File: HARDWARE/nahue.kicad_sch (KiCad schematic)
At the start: 42 parts, among them J1 Conn_01x15, J2 Screw_Terminal_01x03, J3 Screw_Terminal_01x03, J4 Screw_Terminal_01x03, J5 bateria, J6 Screw_Terminal_01x03, J7 Conn_01x15, K1 JQC-3FF-005-1Z, K2 JQC-3FF-005-1Z, K3 JQC-3FF-005-1Z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

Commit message: actualizacion de kicad
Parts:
- removed C2: C_Small, Capacitor_THT:C_Axial_L5.1mm_D3.1mm_P10.00mm_Horizontal, symbol Device:C_Small
- removed U5: KA78M05_TO252, Package_TO_SOT_SMD:TO-252-2, symbol Regulator_Linear:KA78M05_TO252
- added C2: C_Polarized, symbol Device:C_Polarized
- added U5: ESP32-S2-WROVER, RF_Module:ESP32-S2-WROVER, symbol RF_Module:ESP32-S2-WROVER
- added U6: LM7805_TO220, Package_TO_SOT_THT:TO-220-3_Vertical, symbol Regulator_Linear:LM7812_TO220
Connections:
- net +5V: now also C2.2; no longer C1.1
- net D19: now also R4.2; no longer R7.2
- net D21: now also R7.2; no longer R10.1
- net D22: now also R10.1
- net D5: no longer R4.2
- net GND: now also U6.2 (GND); no longer C1.2
- net at J5.2 (Pin_2): now also C1.1
- new net: C2.1, U6.3 (VO)
- new net: C1.2, U6.1 (VI)
- new net: U5.1 (GND), U5.26 (GND), U5.42 (GND), U5.43 (GND)
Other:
- moved on the sheet: C1, J5

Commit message: modificacion del kicad
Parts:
- removed U5: ESP32-S2-WROVER, RF_Module:ESP32-S2-WROVER, symbol RF_Module:ESP32-S2-WROVER
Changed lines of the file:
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@@
-	)
-	(symbol
-		(lib_id "RF_Module:ESP32-S2-WROVER")
-		(at -55.88 48.26 0)
-		(unit 1)
-		(exclude_from_sim no)
-		(in_bom yes)
-		(on_board yes)
-		(dnp no)
-		(fields_autoplaced yes)
-		(property "Reference" "U5"
-			(at -53.7367 15.24 0)
-			(effects
-				(font
-					(size 1.27 1.27)
-				)
-				(justify left)
-			)
-		)
-		(property "Value" "ESP32-S2-WROVER"
-			(at -53.7367 17.78 0)
-			(effects
-				(font
-					(size 1.27 1.27)
-				)
-				(justify left)
-			)
-		)
-		(property "Footprint" "RF_Module:ESP32-S2-WROVER"
-			(at -36.83 77.47 0)
-			(effects
-				(font
-					(size 1.27 1.27)
-				)
-				(hide yes)
-			)
-		)
-		(property "Datasheet" "https://www.espressif.com/sites/default/files/documentation/esp32-s2-wroom_esp32-s2-wroom-i_datasheet_en.pdf"
-			(at -63.5 68.58 0)
-			(effects
-				(font
-					(size 1.27 1.27)
-				)
-				(hide yes)
-			)
-		)
-		(property "Description" "RF Module, ESP32-D0WDQ6 SoC, Wi-Fi 802.11b/g/n, 32-bit, 2.7-3.6V, onboard antenna, SMD"
-			(at -55.88 48.26 0)
-			(effects
-				(font
-					(size 1.27 1.27)
-				)
-				(hide yes)
-			)
-		)
-		(pin "41"
-		)
-		(pin "32"
-		)
-		(pin "30"
-		)
-		(pin "18"
-		)
-		(pin "25"
-		)
-		(pin "22"
-		)
-		(pin "8"
-		)
-		(pin "11"
-		)
-		(pin "2"
-		)
-		(pin "13"
-		)
-		(pin "40"
-		)
-		(pin "36"
-		)
-		(pin "35"
-		)
-		(pin "4"
-		)
-		(pin "26"
-		)
-		(pin "37"
-		)
-		(pin "34"
-		)
-		(pin "27"
-		)
-		(pin "24"
-		)
-		(pin "3"
-		)
-		(pin "17"
-		)
-		(pin "6"
-		)
-		(pin "9"
-		)
-		(pin "16"
-		)
-		(pin "7"
-		)
-		(pin "15"
-		)
-		(pin "19"
-		)
-		(pin "5"
-		)
-		(pin "21"
-		)
-		(pin "10"
-		)
-		(pin "12"
-		)
-		(pin "14"
-		)
-		(pin "43"
-		)
-		(pin "39"
-		)
-		(pin "1"
-		)
-		(pin "42"
-		)
-		(pin "20"
-		)
-		(pin "38"
-		)
-		(pin "33"
-		)
-		(pin "31"
-		)
-		(pin "29"
-		)
-		(pin "28"
-		)
-		(pin "23"
-		)
-		(instances
-			(project ""
-				(path "/0a4955d6-c713-42be-8446-0591522708f4"
-					(reference "U5")
-					(unit 1)
-				)
-			)
-		)
 	)
 	(symbol

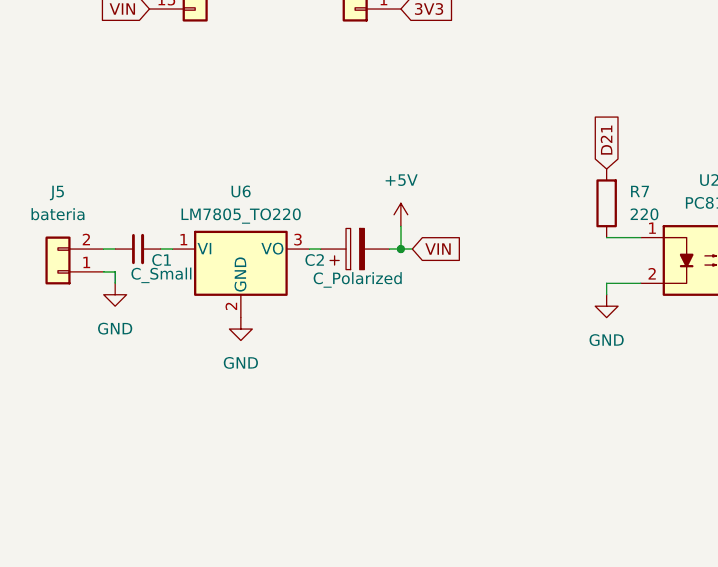
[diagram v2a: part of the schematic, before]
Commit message: modificacion de capacitores pararlelo
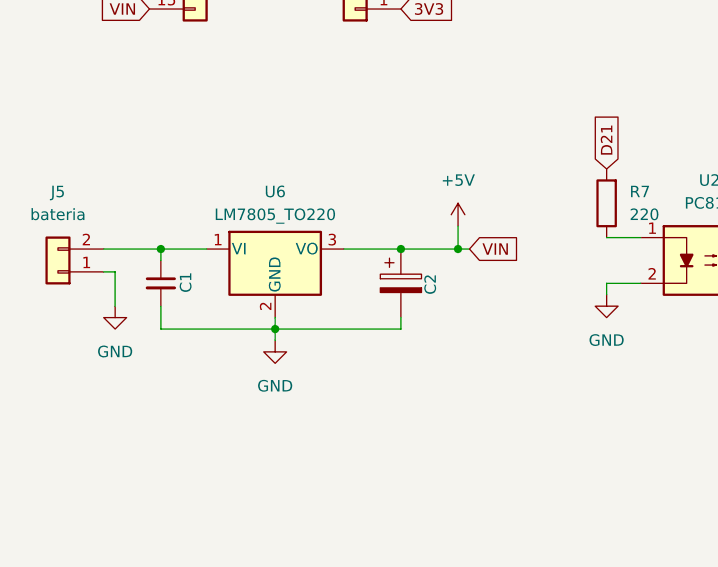
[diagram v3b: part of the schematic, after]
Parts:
- C1: value C_Small -> ~
- C2: value C_Polarized -> ~
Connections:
- net +5V: now also C2.1, U6.3 (VO); no longer C2.2
- net GND: now also C1.2, C2.2
- net at C1.1, J5.2 (Pin_2): now also U6.1 (VI)
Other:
- moved on the sheet: C1, C2, U6

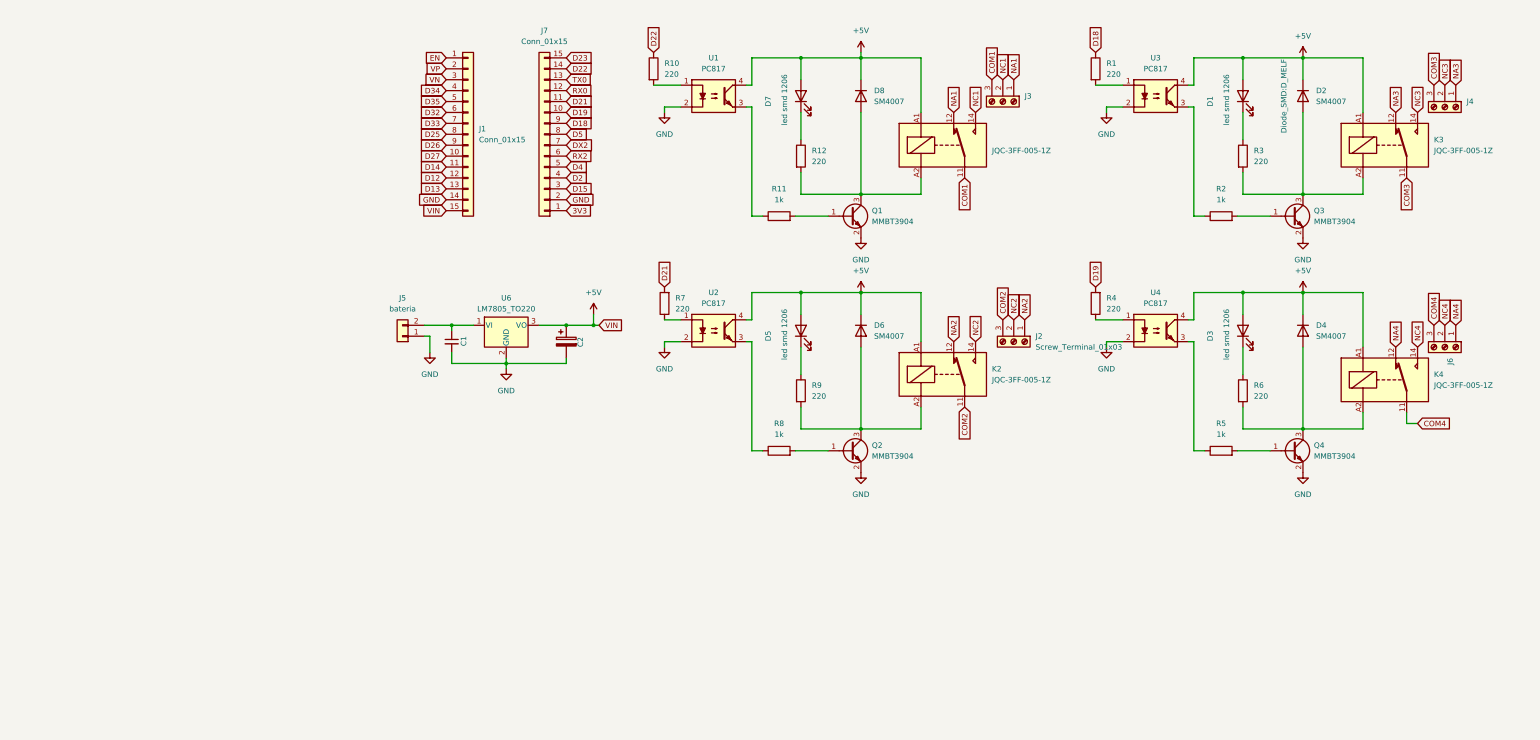
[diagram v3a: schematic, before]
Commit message: se agrego huella del ESP32(falta terminar)
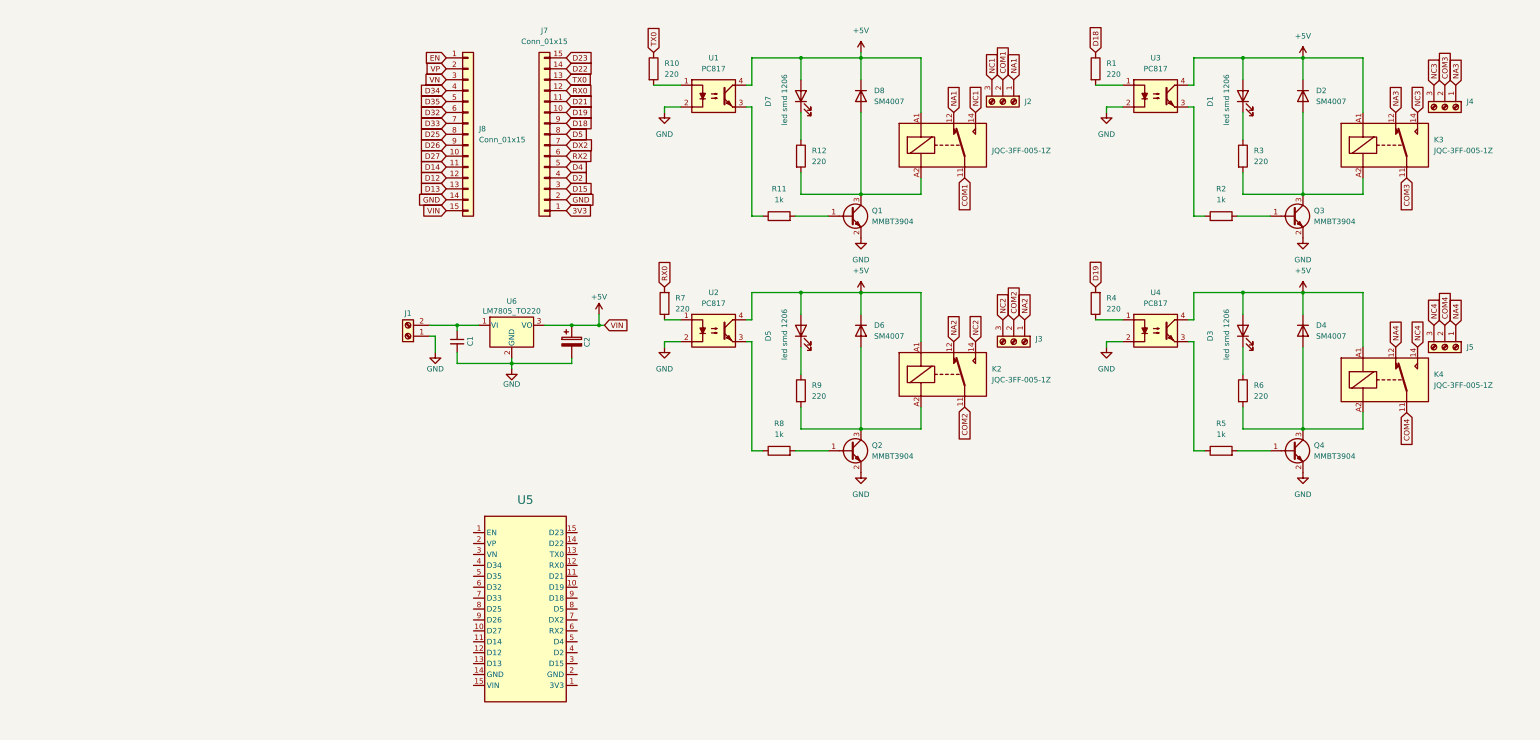
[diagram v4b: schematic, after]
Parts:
- removed J5: bateria, TerminalBlock:TerminalBlock_MaiXu_MX126-5.0-02P_1x02_P5.00mm, symbol Connector_Generic:Conn_01x02
- added J1: ~, TerminalBlock:TerminalBlock_MaiXu_MX126-5.0-02P_1x02_P5.00mm, symbol Connector:Screw_Terminal_01x02
- added U5: ~, esp32-30pines:esp32, symbol ESP32-devkiv v1:ESP32-30pines
- C2: footprint (none) -> Capacitor_THT:CP_Radial_D8.0mm_P3.80mm
- J3: renamed from J2; value Screw_Terminal_01x03 -> ~
- renumbered J3 to J2, J6 to J5, J1 to J8
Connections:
- net COM1: now also J2.2 (Pin_2); no longer J2.3 (Pin_3)
- net COM2: now also J3.2 (Pin_2); no longer J3.3 (Pin_3)
- net COM3: now also J4.2 (Pin_2); no longer J4.3 (Pin_3)
- net COM4: now also J5.2 (Pin_2); no longer J5.3 (Pin_3)
- net D21: no longer R7.2
- net D22: no longer R10.1
- net GND: now also J1.1 (Pin_1)
- net NC1: now also J2.3 (Pin_3); no longer J2.2 (Pin_2)
- net NC2: now also J3.3 (Pin_3); no longer J3.2 (Pin_2)
- net NC3: now also J4.3 (Pin_3); no longer J4.2 (Pin_2)
- net NC4: now also J5.3 (Pin_3); no longer J5.2 (Pin_2)
- net RX0: now also R7.2
- net TX0: now also R10.1
- net at C1.1, U6.1 (VI): now also J1.2 (Pin_2)
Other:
- moved on the sheet: C1, C2, U6

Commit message: últimos arreglos 1
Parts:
- removed J7, J8: Conn_01x15, Connector_PinHeader_2.54mm:PinHeader_1x15_P2.54mm_Vertical, symbol Connector_Generic:Conn_01x15
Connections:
- net +5V: now also U5.15 (VIN)
- net 3V3: now also U5.30 (3V3)
- net D12: now also U5.12 (D12)
- net D13: now also U5.13 (D13)
- net D14: now also U5.11 (D14)
- net D15: now also U5.28 (D15)
- net D18: now also U5.22 (D18)
- net D19: now also U5.21 (D19)
- net D2: now also U5.27 (D2)
- net D21: now also U5.20 (D21)
- net D22: now also U5.17 (D22)
- net D23: now also U5.16 (D23)
- net D25: now also U5.8 (D25)
- net D26: now also U5.9 (D26)
- net D27: now also U5.10 (D27)
- net D32: now also U5.6 (D32)
- net D33: now also U5.7 (D33)
- net D34: now also U5.4 (D34)
- net D35: now also U5.5 (D35)
- net D4: now also U5.26 (D4)
- net D5: now also U5.23 (D5)
- net DX2: now also R7.2, U5.24 (DX2)
- net EN: now also U5.1 (EN)
- net GND: now also U5.14 (GND), U5.29 (GND)
- net RX0: now also U5.19 (RX0); no longer R7.2
- net RX2: now also R10.1, U5.25 (RX2)
- net TX0: now also U5.18 (TX0); no longer R10.1
- net VN: now also U5.3 (VN)
- net VP: now also U5.2 (VP)
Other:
- moved on the sheet: U5

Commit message: retoques del kicad
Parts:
- K1, K2, K3, K4: value JQC-3FF-005-1Z -> RELAY
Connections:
- net DX2: no longer R7.2
- net RX0: now also R10.1
- net RX2: no longer R10.1
- net TX0: now also R7.2
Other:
- note added: "_"
- moved on the sheet: C1, C2, D1, D2, D3, D4, D5, D6, D7, D8, J1, J2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

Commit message: finalizando
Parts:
- added J6: Conn_01x08, Connector_PinSocket_2.54mm:PinSocket_1x08_P2.54mm_Vertical, symbol Connector_Generic:Conn_01x08
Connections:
- net +5V: now also J6.1 (Pin_1)
- net D18: now also R4.2; no longer R1.1
- net D19: now also R1.1; no longer R4.2
- net D2: now also J6.5 (Pin_5)
- net D22: now also J6.2 (Pin_2)
- net D25: now also J6.6 (Pin_6)
- net D32: now also J6.7 (Pin_7)
- net DX2: now also R7.2
- net RX0: now also J6.4 (Pin_4); no longer R10.1
- net RX2: now also R10.1
- net TX0: now also J6.3 (Pin_3); no longer R7.2
- net VP: now also J6.8 (Pin_8)

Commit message: finalizado 2
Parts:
- added SW1: SW, Connector_PinHeader_2.54mm:PinHeader_1x02_P2.54mm_Vertical, symbol Switch:SW_DPST_x2
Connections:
- net D18: no longer R4.2
- net D19: now also R4.2; no longer R1.1
- net D23: now also R1.1
- net at C1.1, U6.1 (VI): now also SW1.2 (B); no longer J1.2 (Pin_2)
- new net: J1.2 (Pin_2), SW1.1 (A)
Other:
- note added: "4 RELAY"
- note added: "CONEXION EXTRA"
- note added: "ESP32"
- note added: "REGULADOR DE TENSION"
- note removed: "_"
- moved on the sheet: C1, C2, J1, U6
